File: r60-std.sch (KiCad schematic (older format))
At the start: 139 parts, among them K0 K_ESC, K0A1 K_0, K0B1 K_MIN, K0C1 K_EQL, K0D1 K_BS, K1 K_1, K10 K_TAB, K11 K_Q, K12 K_W, K13 K_E, K14 K_R, K15 K_T, K16 K_Y, K17 K_U, K18 K_I, K19 K_O, K1A1 K_P, K1B1 K_OBR, K1C1 K_CBR, K1D1 K_BSL, K2 K_2, K20 K_CAP, K21 K_A, K22 K_S, K23 K_D, K24 K_F, K25 K_G, K26 K_H, K27 K_J, K28 K_K, K29 K_L, K2A1 K_COL, K2B1 K_QOT, K2C1 K_ENT, K3 K_3, K30 K_LSH, K31 K_Z, K32 K_X, K33 K_C, K34 K_V, K35 K_B, K36 K_N, K37 K_M, K38 K_COM, K39 K_DOT, K3A1 K_QUE, K3B1 K_RSH, K4 K_4, K40 K_LCL, K41 K_LWN, K42 K_LAL, K45 K_SP, K48 K_RFN, K49 K_RALT, K4A1 K_RWIN, K4B1 K_RCTL, K5 K_5, K6 K_6, K7 K_7, K8 K_8, K9 K_9, P1 USB_B, P2 SPKR, SW1 SW_Push, U1 ATmega32U4-AU, Y1 16MHz

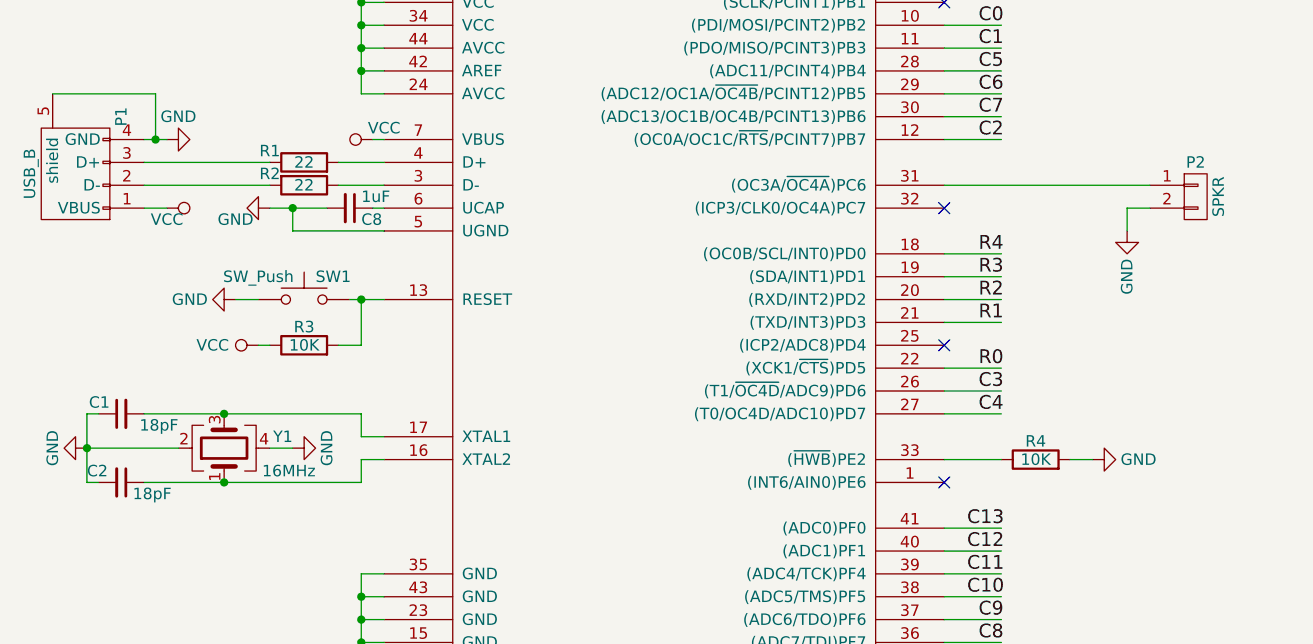
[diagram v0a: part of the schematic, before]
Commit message: Fix silkscreen, move speaker connector, add speaker hardware
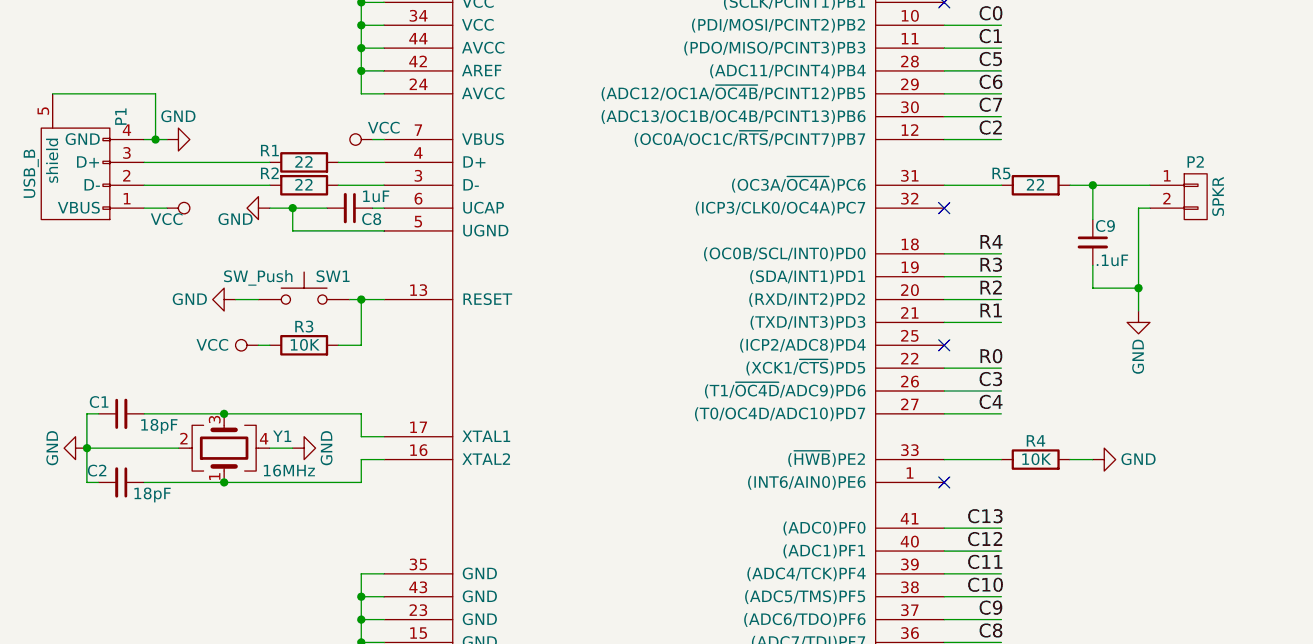
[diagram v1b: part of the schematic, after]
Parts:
- added C9: .1uF, Capacitors_SMD:C_0805_HandSoldering, symbol C_Small
- added R5: 22, Resistors_SMD:R_0805_HandSoldering, symbol R
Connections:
- wire segments 219 -> 223
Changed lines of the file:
@@
 encoding utf-8
 Sheet 1 1
-Title ""
+Title "Standard 60% PCB"
 Date "2017-06-04"
-Rev "1A"
+Rev "1.2"
 Comp ""
 Comment1 ""
@@
 $EndComp
 $Comp
-L VCC #PWR01
+L VCC #PWR1
 U 1 1 59339969
 P 2350 4600
-F 0 "#PWR01" H 2350 4450 50  0001 C CNN
+F 0 "#PWR1" H 2350 4450 50  0001 C CNN
 F 1 "VCC" H 2350 4750 50  0000 C CNN
 F 2 "" H 2350 4600 50  0000 C CNN
@@
 $EndComp
 $Comp
-L GND #PWR02
+L GND #PWR14
 U 1 1 59339A58
 P 2350 7600
-F 0 "#PWR02" H 2350 7350 50  0001 C CNN
+F 0 "#PWR14" H 2350 7350 50  0001 C CNN
 F 1 "GND" H 2350 7450 50  0000 C CNN
 F 2 "" H 2350 7600 50  0000 C CNN
@@
 $EndComp
 $Comp
-L GND #PWR03
+L GND #PWR12
 U 1 1 59339B8E
 P 2050 6700
-F 0 "#PWR03" H 2050 6450 50  0001 C CNN
+F 0 "#PWR12" H 2050 6450 50  0001 C CNN
 F 1 "GND" H 2050 6550 50  0000 C CNN
 F 2 "" H 2050 6700 50  0000 C CNN
@@
 $EndComp
 $Comp
-L GND #PWR04
+L GND #PWR11
 U 1 1 59339B9F
 P 1150 6700
-F 0 "#PWR04" H 1150 6450 50  0001 C CNN
+F 0 "#PWR11" H 1150 6450 50  0001 C CNN
 F 1 "GND" H 1150 6550 50  0000 C CNN
 F 2 "" H 1150 6700 50  0000 C CNN
@@
 $EndComp
 $Comp
-L VCC #PWR05
+L VCC #PWR9
 U 1 1 59339FD8
 P 1900 6250
-F 0 "#PWR05" H 1900 6100 50  0001 C CNN
+F 0 "#PWR9" H 1900 6100 50  0001 C CNN
 F 1 "VCC" V 1900 6450 50  0000 C CNN
 F 2 "" H 1900 6250 50  0000 C CNN
@@
 $EndComp
 $Comp
-L GND #PWR06
+L GND #PWR7
 U 1 1 5933A5D1
 P 1800 6050
-F 0 "#PWR06" H 1800 5800 50  0001 C CNN
+F 0 "#PWR7" H 1800 5800 50  0001 C CNN
 F 1 "GND" V 1800 5850 50  0000 C CNN
 F 2 "" H 1800 6050 50  0000 C CNN
@@
 $EndComp
 $Comp
-L VCC #PWR07
+L VCC #PWR4
 U 1 1 5933AEA7
 P 1500 5650
-F 0 "#PWR07" H 1500 5500 50  0001 C CNN
+F 0 "#PWR4" H 1500 5500 50  0001 C CNN
 F 1 "VCC" V 1550 5650 50  0000 C CNN
 F 2 "" H 1500 5650 50  0000 C CNN
@@
 $EndComp
 $Comp
-L VCC #PWR08
+L VCC #PWR3
 U 1 1 5933AF29
 P 2400 5350
-F 0 "#PWR08" H 2400 5200 50  0001 C CNN
+F 0 "#PWR3" H 2400 5200 50  0001 C CNN
 F 1 "VCC" V 2450 5300 50  0000 C CNN
 F 2 "" H 2400 5350 50  0000 C CNN
@@
 $EndComp
 $Comp
-L GND #PWR09
+L GND #PWR2
 U 1 1 5933AF87
 P 1500 5350
-F 0 "#PWR09" H 1500 5100 50  0001 C CNN
+F 0 "#PWR2" H 1500 5100 50  0001 C CNN
 F 1 "GND" V 1600 5300 50  0000 C CNN
 F 2 "" H 1500 5350 50  0000 C CNN
@@
 $EndComp
 $Comp
-L GND #PWR010
+L GND #PWR5
 U 1 1 5933B07D
 P 1950 5650
-F 0 "#PWR010" H 1950 5400 50  0001 C CNN
+F 0 "#PWR5" H 1950 5400 50  0001 C CNN
 F 1 "GND" V 2000 5500 50  0000 C CNN
 F 2 "" H 1950 5650 50  0000 C CNN
@@
 $EndComp
 $Comp
-L GND #PWR011
+L GND #PWR13
 U 1 1 5933D359
 P 5550 6750
-F 0 "#PWR011" H 5550 6500 50  0001 C CNN
+F 0 "#PWR13" H 5550 6500 50  0001 C CNN
 F 1 "GND" V 5550 6550 50  0000 C CNN
 F 2 "" H 5550 6750 50  0000 C CNN
@@
 $EndComp
 $Comp
-L GND #PWR012
+L GND #PWR10
 U 1 1 5933E10F
 P 7150 6250
-F 0 "#PWR012" H 7150 6000 50  0001 C CNN
+F 0 "#PWR10" H 7150 6000 50  0001 C CNN
 F 1 "GND" H 7150 6100 50  0000 C CNN
 F 2 "" H 7150 6250 50  0000 C CNN
@@
 $EndComp
 $Comp
-L VCC #PWR013
+L VCC #PWR6
 U 1 1 5933E360
 P 7150 5750
-F 0 "#PWR013" H 7150 5600 50  0001 C CNN
+F 0 "#PWR6" H 7150 5600 50  0001 C CNN
 F 1 "VCC" H 7150 5900 50  0000 C CNN
 F 2 "" H 7150 5750 50  0000 C CNN
@@
 $EndComp
 $Comp
-L GND #PWR014
+L GND #PWR8
 U 1 1 596F83D7
-P 5700 5750
-F 0 "#PWR014" H 5700 5500 50  0001 C CNN
-F 1 "GND" V 5700 5550 50  0000 C CNN
-F 2 "" H 5700 5750 50  0000 C CNN
-F 3 "" H 5700 5750 50  0000 C CNN
-	1    5700 5750
+P 5750 6100
+F 0 "#PWR8" H 5750 5850 50  0001 C CNN
+F 1 "GND" V 5750 5900 50  0000 C CNN
+F 2 "" H 5750 6100 50  0000 C CNN
+F 3 "" H 5750 6100 50  0000 C CNN
+	1    5750 6100
 	1    0    0    -1
 $EndComp
@@
 	2450 6750 2350 6750
 Wire Wire Line
-	2350 6750 2350 6850
-Wire Wire Line
-	2350 6850 1400 6850
+	2350 6850 2350 6750
+Wire Wire Line
+	1400 6850 2350 6850
 Wire Wire Line
 	1200 6550 1150 6550
@@
 Connection ~ 2650 2950
 Wire Wire Line
-	4900 5550 5800 5550
-Wire Wire Line
-	5800 5650 5700 5650
-Wire Wire Line
-	5700 5650 5700 5750
-Wire Wire Line
 	4900 4850 5150 4850
 Connection ~ 1450 950
@@
 NoConn ~ 4900 6850
 NoConn ~ 4900 4750
+$Comp
+L R R5
+U 1 1 599CD69A
+P 5300 5550
+F 0 "R5" V 5350 5700 50  0000 C CNN
+F 1 "22" V 5300 5550 50  0000 C CNN
+F 2 "Resistors_SMD:R_0805_HandSoldering" V 5230 5550 50  0001 C CNN
+F 3 "" H 5300 5550 50  0000 C CNN
+	1    5300 5550
+	0    -1   -1   0
+$EndComp
+$Comp
+L C_Small C9
+U 1 1 599CE37E
+P 5550 5800
+F 0 "C9" H 5560 5870 50  0000 L CNN
+F 1 ".1uF" H 5560 5720 50  0000 L CNN
+F 2 "Capacitors_SMD:C_0805_HandSoldering" H 5550 5800 50  0001 C CNN
+F 3 "" H 5550 5800 50  0000 C CNN
+	1    5550 5800
+	1    0    0    -1
+$EndComp
+Wire Wire Line
+	4900 5550 5150 5550
+Wire Wire Line
+	5450 5550 5800 5550
+Wire Wire Line
+	5550 5700 5550 5550
+Connection ~ 5550 5550
+Wire Wire Line
+	5550 5900 5550 6000
+Wire Wire Line
+	5550 6000 5750 6000
+Wire Wire Line
+	5800 5650 5750 5650
+Wire Wire Line
+	5750 5650 5750 6100
+Connection ~ 5750 6000
 $EndSCHEMATC

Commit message: start on r2.0 board
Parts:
- C1, C2, C3, C4, C5, C6, C7, C8, C9: footprint Capacitors_SMD:C_0805_HandSoldering -> Capacitors_SMD:C_0805
- D0, D0A1, D0B1, D0C1, D0D1, D1, D10, D11, D12, D13, D14, D15, D16, D17, D18, D19, D1A1, D1B1, D1C1, D1D1, D2, D20, D21, D22, D23, D24, D25, D26, D27, D28, D29, D2A1, D2B1, D2C1, D3, D30, D31, D32, D33, D34, D35, D36, D37, D38, D39, D3A1, D3B1, D4, D40, D41, D42, D45, D48, D49, D4A1, D4B1, D5, D6, D7, D8, D9: footprint Diodes_THT:D_A-405_P7.62mm_Horizontal -> Diodes_SMD:D_SOD-323
- R1, R2, R3, R4, R5: footprint Resistors_SMD:R_0805_HandSoldering -> Resistors_SMD:R_0805
- Y1: footprint Crystals:Crystal_SMD_3225-4pin_3.2x2.5mm_HandSoldering -> Crystals:Crystal_SMD_3225-4pin_3.2x2.5mm

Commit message: switch to 0805 diodes
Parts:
- D0, D0A1, D0B1, D0C1, D0D1, D1, D10, D11, D12, D13, D14, D15, D16, D17, D18, D19, D1A1, D1B1, D1C1, D1D1, D2, D20, D21, D22, D23, D24, D25, D26, D27, D28, D29, D2A1, D2B1, D2C1, D3, D30, D31, D32, D33, D34, D35, D36, D37, D38, D39, D3A1, D3B1, D4, D40, D41, D42, D45, D48, D49, D4A1, D4B1, D5, D6, D7, D8, D9: footprint Diodes_SMD:D_SOD-323 -> Diodes_SMD:D_0805

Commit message: Expand out 0805 pads on both r and d
re-route some traces as a consequence.
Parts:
- D0, D0A1, D0B1, D0C1, D0D1, D1, D10, D11, D12, D13, D14, D15, D16, D17, D18, D19, D1A1, D1B1, D1C1, D1D1, D2, D20, D21, D22, D23, D24, D25, D26, D27, D28, D29, D2A1, D2B1, D2C1, D3, D30, D31, D32, D33, D34, D35, D36, D37, D38, D39, D3A1, D3B1, D4, D40, D41, D42, D45, D48, D49, D4A1, D4B1, D5, D6, D7, D8, D9: footprint Diodes_SMD:D_0805 -> Keyboard:D_0805
- R1, R2, R3, R4, R5: footprint Resistors_SMD:R_0805 -> Keyboard:RC_0805

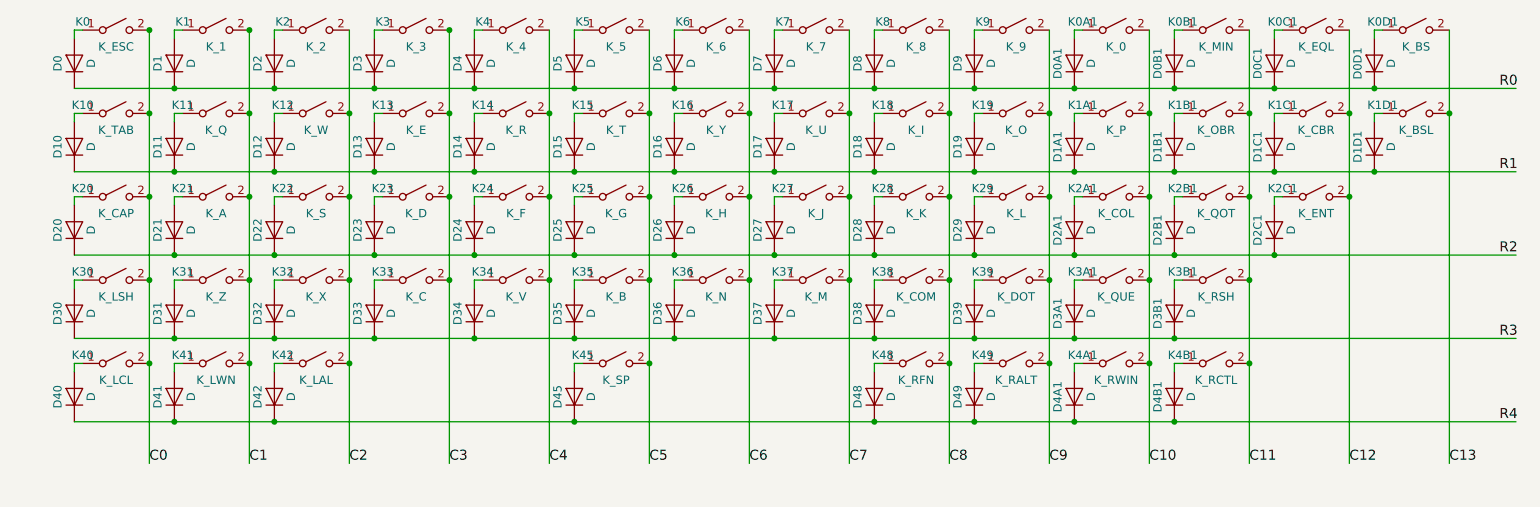
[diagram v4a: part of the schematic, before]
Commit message: add ISO and stepped capslock support
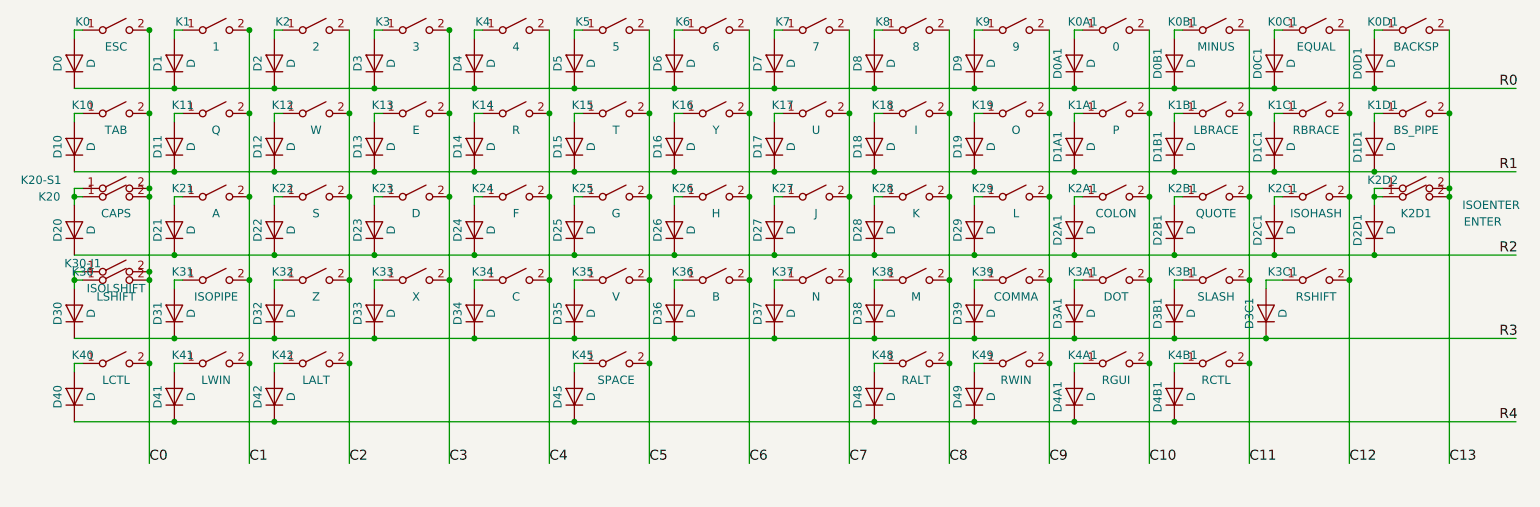
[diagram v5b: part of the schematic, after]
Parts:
- added D2D1, D3C1: D, Keyboard:D_0805, symbol D
- added K20-S1: CAPS, Keyboard:CHERRY_PCB_125H, symbol SW_SPST
- added K2D1: ENTER, Keyboard:CHERRY_PCB_225H, symbol SW_SPST
- added K2D2: ISOENTER, Keyboard:CHERRY_PCB_200H, symbol SW_SPST
- added K30-I1: ISOLSHIFT, Keyboard:CHERRY_PCB_125H, symbol SW_SPST
- added K3C1: RSHIFT, Keyboard:CHERRY_PCB_275H, symbol SW_SPST
- K0: value K_ESC -> ESC
- K0A1: value K_0 -> 0
- K0B1: value K_MIN -> MINUS
- K0C1: value K_EQL -> EQUAL
- K0D1: value K_BS -> BACKSP
- K1: value K_1 -> 1
- K10: value K_TAB -> TAB
- K11: value K_Q -> Q
- K12: value K_W -> W
- K13: value K_E -> E
- K14: value K_R -> R
- K15: value K_T -> T
- K16: value K_Y -> Y
- K17: value K_U -> U
- K18: value K_I -> I
- K19: value K_O -> O
- K1A1: value K_P -> P
- K1B1: value K_OBR -> LBRACE
- K1C1: value K_CBR -> RBRACE
- K1D1: value K_BSL -> BS_PIPE
- K2: value K_2 -> 2
- K20: value K_CAP -> CAPS
- K21: value K_A -> A
- K22: value K_S -> S
- K23: value K_D -> D
- K24: value K_F -> F
- K25: value K_G -> G
- K26: value K_H -> H
- K27: value K_J -> J
- K28: value K_K -> K
- K29: value K_L -> L
- K2A1: value K_COL -> COLON
- K2B1: value K_QOT -> QUOTE
- K2C1: value K_ENT -> ISOHASH; footprint Keyboard:CHERRY_PCB_225H -> Keyboard:CHERRY_PCB_100H
- K3: value K_3 -> 3
- K30: value K_LSH -> LSHIFT
- K31: value K_Z -> ISOPIPE
- K32: value K_X -> Z
- K33: value K_C -> X
- K34: value K_V -> C
- K35: value K_B -> V
- K36: value K_N -> B
- K37: value K_M -> N
- K38: value K_COM -> M
- K39: value K_DOT -> COMMA
- K3A1: value K_QUE -> DOT
- K3B1: value K_RSH -> SLASH; footprint Keyboard:CHERRY_PCB_275H -> Keyboard:CHERRY_PCB_100H
- K4: value K_4 -> 4
- K40: value K_LCL -> LCTL
- K41: value K_LWN -> LWIN
- K42: value K_LAL -> LALT
- K45: value K_SP -> SPACE
- K48: value K_RFN -> RALT
- K49: value K_RALT -> RWIN
- K4A1: value K_RWIN -> RGUI
- K4B1: value K_RCTL -> RCTL
- K5: value K_5 -> 5
- K6: value K_6 -> 6
- K7: value K_7 -> 7
- K8: value K_8 -> 8
- K9: value K_9 -> 9
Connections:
- wire segments 223 -> 230

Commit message: First pass at r4 design
Remove ISO layouts, keep stepped capslock/ctrl.  Allow for
either 6.25u space or 1.25/2.25/2.75 split space. Move to
0603 footprints near atmega to handle smaller space due to
split spacebar.  Switch atmega from -AU in 44 TQFP to -MU
part in 44 QFN, again to deal with less room due to split
spacebar.
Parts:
- removed D2C1, D3C1: D, Keyboard:D_0805, symbol D
- removed K2C1: ISOHASH, Keyboard:CHERRY_PCB_100H, symbol SW_SPST
- removed K2D2: ISOENTER, Keyboard:CHERRY_PCB_200H, symbol SW_SPST
- removed K30-I1: ISOLSHIFT, Keyboard:CHERRY_PCB_125H, symbol SW_SPST
- removed K3C1: RSHIFT, Keyboard:CHERRY_PCB_275H, symbol SW_SPST
- removed P2: SPKR, Pin_Headers:Pin_Header_Straight_1x02_Pitch2.54mm, symbol CONN_01X02
- added D43, D44: D, Keyboard:D_0805, symbol D
- added K43: LFN, Keyboard:CHERRY_PCB_125H, symbol SW_SPST
- added K44: SSPACE-1, Keyboard:CHERRY_PCB_225H, symbol SW_SPST
- added K45-1: SSPACE-2, Keyboard:CHERRY_PCB_275H, symbol SW_SPST
- added LS1: AST1109MLT, Keyboard:AST1109ML-SMT, symbol AST1109MLT
- C1, C2, C3, C4, C5, C6, C7, C8: footprint Capacitors_SMD:C_0805 -> Capacitors_SMD:C_0603
- K0D1: footprint Keyboard:CHERRY_PCB_200H -> Keyboard:CHERRY_PCB_200H_INVERTED
- K31: value ISOPIPE -> Z
- K32: value Z -> x
- K33: value X -> C
- K34: value C -> V
- K35: value V -> B
- K36: value B -> N
- K37: value N -> M
- K38: value M -> COMMA
- K39: value COMMA -> DOT
- K3A1: value DOT -> SLASH
- K3B1: value SLASH -> RSHIFT; footprint Keyboard:CHERRY_PCB_100H -> Keyboard:CHERRY_PCB_275H
- R4: footprint Keyboard:RC_0805 -> Resistors_SMD:R_0603
- U1: footprint Housings_QFP:TQFP-44_10x10mm_Pitch0.8mm -> Housings_DFN_QFN:QFN-44-1EP_7x7mm_Pitch0.5mm
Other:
- moved on the sheet: C3, C4, C5, C6, C7
